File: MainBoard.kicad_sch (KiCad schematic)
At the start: 113 parts, among them J1 Power from Back_Board, J10 Conn_01x08_Socket, J11 GH-S37D, J12 LoadCell, J13 LoadCell, J2 UnitV01, J20 to LED, J3 to LED, J4 to Tile_Board, J5 to LiDAR_Board, J6 ST-Link, J7 ST-Link, J8 UnitV02, J9 GH-S37D, M1 STS3032, M2 STS3032, M3 STS3032, M4 STS3032, SW1 RESET_SWITCH, SW2 RESET_SWITCH, SW3 MODE_SWITCH, SW4 MODE_SWITCH, SW5 B-12CCP, U1 LT1085CM-3.3#PBF, U10 NJU77551F, U11 XIAO ESP32C3, U12 XIAO-RP2040-DIP, U2 STM32F446RET6, U3 BNO085, U4 AE-BNO055-BO, U5 STM32H723ZGT6, U8 NJU77551F, U9 MAX3485

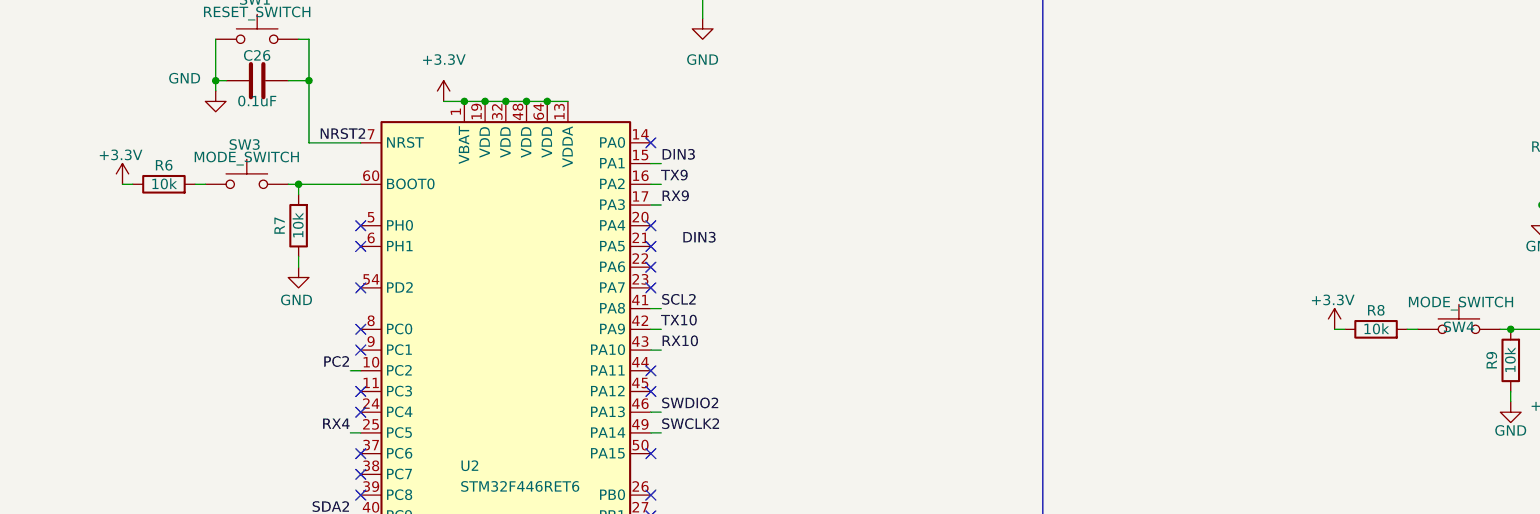
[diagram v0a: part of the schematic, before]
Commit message: LiDAR基板Rev.3コネクタ配置
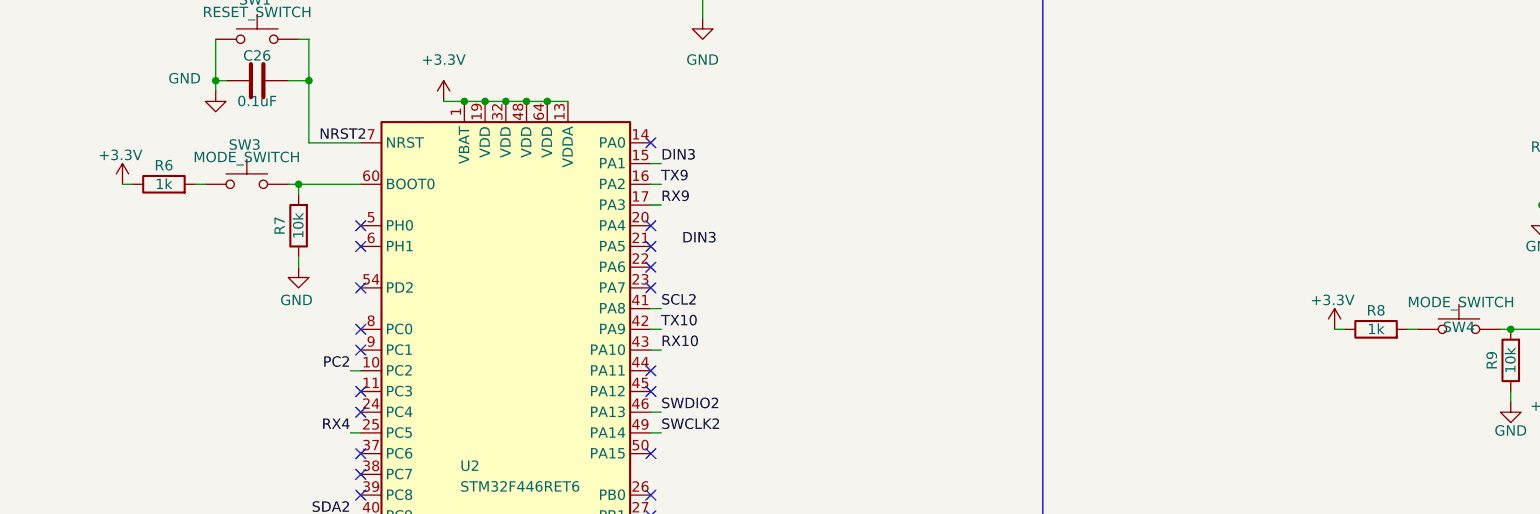
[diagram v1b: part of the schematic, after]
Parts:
- R6, R8: value 10k -> 1k

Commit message: メイン基板Rev.3
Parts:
- added IC1, IC2: R3111N211A-TR-FE, R3111N211A:SOT95P280X130-5N, symbol R3111N211A:R3111N211A-TR-FE
- added R37, R40: 5.6k, Resistor_SMD:R_0402_1005Metric, symbol Device:R
- added R38, R42: 2.4k, Resistor_SMD:R_0402_1005Metric, symbol Device:R
- added R39, R41: 470k, Resistor_SMD:R_0402_1005Metric, symbol Device:R
- renumbered C49 to C31, C48 to C32, C50 to C33, C51 to C34, C31 to C35, C32 to C36, C52 to C37, C53 to C38, C33 to C39, C54 to C40, C55 to C41, J9 to J10, J10 to J11, J11 to J12, J12 to J13, J13 to J14, J20 to J9, R15 to R14, R16 to R15, R17 to R16, R18 to R17, R19 to R18, R20 to R19, R21 to R20, R22 to R21, R24 to R22, R25 to R23, R27 to R24, R28 to R25, R23 to R26, R26 to R27
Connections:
- net +3.3V: now also R39.1, R41.1
- net +7.5V: now also R37.1, R40.1
- net DIN1: no longer D3.4 (DIN)
- net GND: now also IC1.3 (GND), IC2.3 (GND), R38.2, R42.2
- net NRST: now also IC1.1 (OUT), R39.2
- net NRST2: now also IC2.1 (OUT), R41.2
- net at D2.2 (DOUT): now also D3.4 (DIN)
- new net: IC2.2 (VDD), R40.2, R42.1
- new net: IC1.2 (VDD), R37.2, R38.1
- no-connect marks 168 -> 167
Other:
- moved on the sheet: D3, D4

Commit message: 後ろ基板Rev.2
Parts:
- removed R13: 1k, Resistor_SMD:R_0402_1005Metric, symbol Device:R
- removed SW5: B-12CCP, B-12CCP:B-12CCP, symbol B-12CCP:B-12CCP
- added SW10: START_SWITCH, B12AP_NKK:B12AP_NKK, symbol Switch:SW_SPDT
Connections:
- net GND: now also SW10.3 (C)
- net at R12.2: now also SW10.1 (A)
- net at U2.33 (PB12): now also SW10.2 (B)
- no-connect marks 167 -> 168
